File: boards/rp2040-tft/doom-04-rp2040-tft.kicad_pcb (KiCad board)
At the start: 4 copper layers, 132 x 58 mm, 79 parts, among them J2 S2B-PH-K-S(LF)(SN), J4 DM3AT-SF-PEJM5, J5 S2B-PH-K-S(LF)(SN), Q1 FS8205A, SW9 JS102011SAQN, U1 RP2040, U2 TP4056, U3 DW01A, U4 TLV75533PDBVR, U5 PAM8403DR, U6 W25Q128JVSIQ, U7 ESD 2-line, Y1 12MHz 10pF

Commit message: PCBKit's mark and pcbkit.io on every board; the RP2350 handheld ready to order
The handheld runs from two 18650 cells in parallel behind a DW01A protector and a reverse-cell
P-MOSFET, charged at up to 500 mA from the Pico's USB-C by a BQ24075 (power path into VSYS, timers
off for 6 Ah), with an on/off switch on 3V3_EN, M3 holes, ground pours and the console on pads.
Every assembled part has a JLCPCB code in stock (Basic where there is one); the module sockets are
in the BOM, the modules listed in the order's README. Check complete, the ready review clean.
Every board: routed and checked complete with the new mark.
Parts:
- added logo: , Logo_PCBKit_pcbkit.io, F.Cu at (127.8, 194.8)
- SW1, SW10, SW2, SW3, SW4, SW5, SW6, SW7, SW8: value (none) -> PTS645SM43SMTR92 LFS

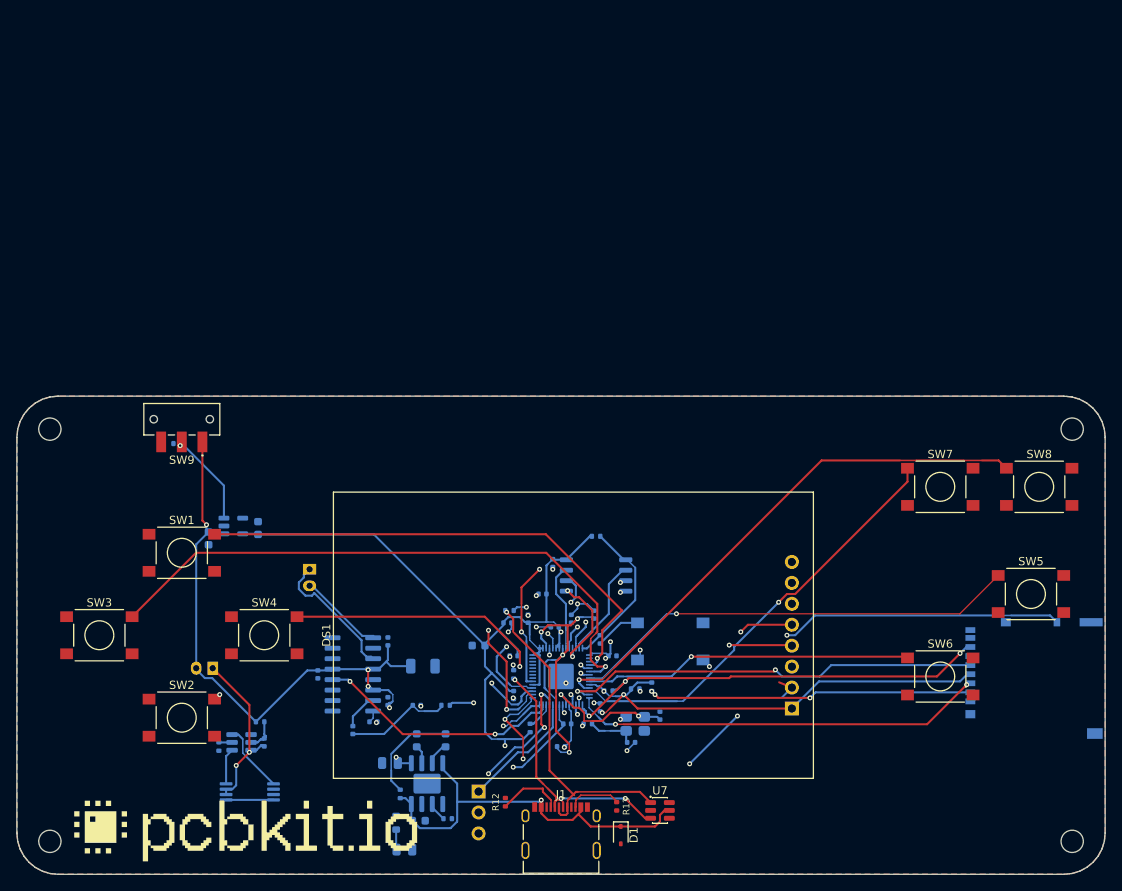
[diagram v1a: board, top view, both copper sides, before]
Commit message: rp2040-tft: two 18650 cells with protection and a USB-C charger; every part orderable
The LiPo and TP4056 become two 18650 in parallel (Keystone 1042 holders on the back) behind a
reverse-cell P-FET and DW01A + FS8205A, charged by a BQ24075 with power path from the board's
USB-C (1 A PTC and TVS on VBUS), SYS feeding the LDO and the amplifier (as rp2350-handheld).
BOOT and RESET buttons by the USB-C for the boot ROM's UF2 loader; the RP2040's decoupling within
3 mm of each supply pin; the speaker connector on the edge; board 132 x 104 mm, M3 holes, test
pads; every assembled part pinned to an LCSC code.
check: complete, 0 errors (4 USB-pair warnings, justified); ready lens: nothing to fix; fab
export without --force.

Claude-Session: https://claude.ai/code/session_01ATmMmxyrWxFwR3nTdXUrcx
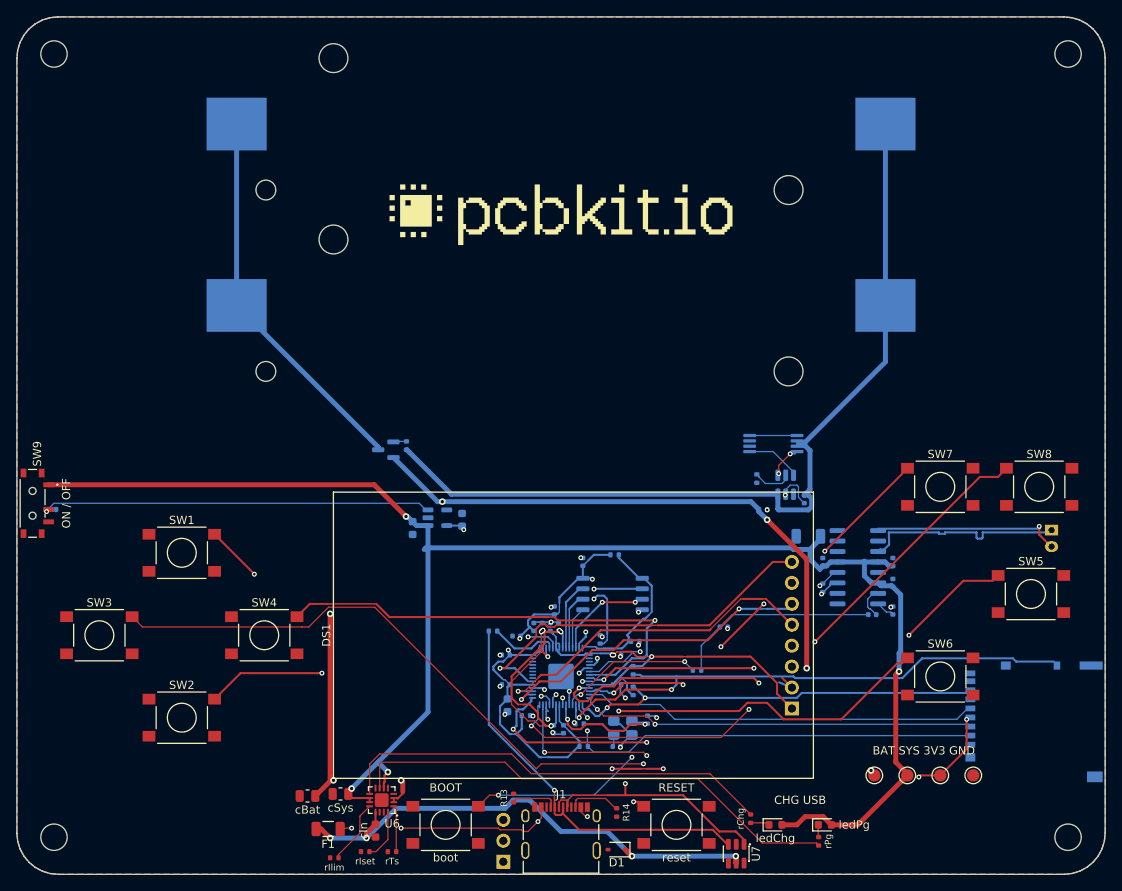
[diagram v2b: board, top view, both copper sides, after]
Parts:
- removed C20: 10uF, C_0805_2012Metric
- removed C21: 100nF, C_0402_1005Metric
- removed C8: 1uF, C_0603_1608Metric
- removed D2: red, LED_0603_1608Metric
- removed D3: green, LED_0603_1608Metric
- removed J2: S2B-PH-K-S(LF)(SN), JST_PH_S2B-PH-K_1x02_P2.00mm_Horizontal
- removed R18, R5: 1kohm, R_0402_1005Metric
- removed SW10: PTS645SM43SMTR92 LFS, SW_Tactile_SPST_6x6mm_SMD
- added BT1: 1042, BatteryHolder_Keystone_1042_1x18650, B.Cu at (166.0, 131.0)
- added BT2: 1042, BatteryHolder_Keystone_1042_1x18650, B.Cu at (166.0, 109.0)
- added F1: PTC 1000mA, Fuse_1206_3216Metric, F.Cu at (137.8, 194.5)
- added Q2: FS8205A, TSSOP-8_4.4x2.93mm_P0.65mm, B.Cu at (191.8, 147.8)
- added boot: PTS645SM43SMTR92 LFS, SW_Tactile_SPST_6x6mm_SMD, F.Cu at (152.0, 194.0)
- added cBat: 4.7uF, C_0805_2012Metric, F.Cu at (135.2, 190.5)
- added cIn: 1uF, C_0603_1608Metric, F.Cu at (143.5, 194.7)
- added cSys: 4.7uF, C_0805_2012Metric, F.Cu at (139.2, 190.2)
- added ledChg: red, LED_0603_1608Metric, F.Cu at (192.0, 194.0)
- added ledPg: green, LED_0603_1608Metric, F.Cu at (198.0, 194.0)
- added rBoot: 1kohm, R_0402_1005Metric, B.Cu at (175.0, 171.8)
- added rChg: 1.5kohm, R_0402_1005Metric, F.Cu at (189.0, 193.2)
- added rIlim: 1.18kohm, R_0402_1005Metric, F.Cu at (138.5, 198.0)
- added rIset: 1.13kohm, R_0402_1005Metric, F.Cu at (142.2, 197.2)
- added rPg: 1.5kohm, R_0402_1005Metric, F.Cu at (197.2, 196.0)
- added rTs: 10kohm, R_0402_1005Metric, F.Cu at (145.5, 197.2)
- added reset: PTS645SM43SMTR92 LFS, SW_Tactile_SPST_6x6mm_SMD, F.Cu at (180.0, 194.0)
- added tpBat: , TestPoint_Round_D1.5mm, F.Cu at (204.0, 188.0)
- added tpGnd: , TestPoint_Round_D1.5mm, F.Cu at (216.0, 188.0)
- added tpSys: , TestPoint_Round_D1.5mm, F.Cu at (208.0, 188.0)
- added tpV3: , TestPoint_Round_D1.5mm, F.Cu at (212.0, 188.0)
- C19: value 10uF -> 100nF; footprint C_0805_2012Metric -> C_0402_1005Metric
- H1, H2, H3, H4: footprint MountingHole_2.7mm_M2.5 -> MountingHole_3.2mm_M3
- Q1: value FS8205A -> AO3401A; footprint TSSOP-8_4.4x2.93mm_P0.65mm -> SOT-23
- R12: value 5.1kohm -> 100kohm; moved to B.Cu
- R14: value 1ohm -> 5.1kohm; footprint R_0603_1608Metric -> R_0402_1005Metric; moved to F.Cu
- R15: value 1.2kohm -> 100kohm
- R16: value 1kohm -> 100ohm
- R17: value 100ohm -> 1kohm
- SW9: value JS102011SAQN -> MSK12C02; footprint SW_Slide_SPDT_CK_JS102011SAQN_Horizontal -> SW_Slide_SPDT_Shouhan_MSK12C02
- U2: value TP4056 -> DW01A; footprint SOIC-8-1EP_3.9x4.9mm_P1.27mm_EP2.413x3.302mm -> SOT-6_1.6x2.9mm_P0.95mm
- U3: value DW01A -> W25Q128JVSIQ; footprint SOT-6_1.6x2.9mm_P0.95mm -> SOIC-8_5.23x5.28mm_P1.27mm
- U6: value W25Q128JVSIQ -> BQ24075RGTR; footprint SOIC-8_5.23x5.28mm_P1.27mm -> QFN-16-1EP_3x3mm_P0.5mm_EP1.68x1.68mm; moved to F.Cu
- moved J5 90.1 mm to (225.5, 159.2)
- moved logo 84.0 mm to (166.0, 120.0)
- moved R17 67.1 mm to (189.8, 152.0), turned to 90 degrees
- moved C29 64.5 mm to (203.8, 168.5), turned to 180 degrees
- moved C19 64.5 mm to (195.5, 154.5), turned to 270 degrees
- moved C28 64.4 mm to (206.2, 168.0), turned to 270 degrees
- moved C24 62.9 mm to (206.2, 164.7)
- moved C26 62.7 mm to (197.8, 162.1), turned to 270 degrees
- moved U5 62.6 mm to (202.0, 162.8)
- moved C25 62.0 mm to (206.2, 162.1)
- moved U2 56.6 mm to (193.2, 152.8), turned to 90 degrees
- moved R16 55.9 mm to (190.5, 155.8), turned to 180 degrees
- moved C27 49.3 mm to (196.0, 159.0), turned to 0 degrees
- moved U3 48.5 mm to (172.2, 166.0), turned to 0 degrees
- moved R12 46.5 mm to (197.8, 165.2)
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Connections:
- net Net-(C11-1) renamed DVDD
- C19 pad 1: U2Support/C1_P -> Net-(C19-1)
- C19 pad 2: GND -> CELL_N
- C22 pad 1: VBAT -> SYS
- C24 pad 1: VBAT -> SYS
- C25 pad 1: VBAT -> SYS
- C26 pad 1: VBAT -> SYS
- C27 pad 1: VBAT -> SYS
- C29 pad 1: Net-(C29-1) -> AUDIO
- C29 pad 2: AUDIO -> Net-(C29-1)
- J1 pad A4: VBUS -> usb/power/raw
- J1 pad B4: VBUS -> usb/power/raw
- Q1 pad 1: U3Support/DRAIN -> reversed/gate
- Q1 pad 2: BAT_N -> BAT
- Q1 pad 3: BAT_N -> BAT_IN
- R12 pad 1: usb/power/cc1 -> AMP_SD
- R13 pad 1: usb/power/cc2 -> usb/power/cc1
- R14 pad 1: VBUS -> usb/power/cc2
- R14 pad 2: U2Support/C1_P -> GND
- R15 pad 1: Net-(R15-1) -> CELL_N
- R15 pad 2: GND -> reversed/gate
- R16 pad 1: U2Support/LED_A -> BAT
- R16 pad 2: VBUS -> Net-(C19-1)
- R17 pad 1: Net-(C21-1) -> Net-(R17-1)
- R17 pad 2: VBAT -> GND
- R6 pad 1: Net-(R6-1) -> V3
- R6 pad 2: V3 -> RUN
- R8 pad 1: SD_CS -> V3
- R8 pad 2: V3 -> SD_CS
- R9 pad 1: SD_MISO -> V3
- R9 pad 2: V3 -> SD_MISO
- SW9 pad 1: VBAT -> SYS
- SW9 pad 3: GND -> (no net)
- U1 pad 26: Net-(R6-1) -> RUN
- U2 pad 1: GND -> Net-(Q2-4)
- U2 pad 2: Net-(R15-1) -> Net-(R17-1)
- U2 pad 3: GND -> Net-(Q2-5)
- U2 pad 4: VBUS -> (no net)
- U2 pad 5: VBAT -> Net-(C19-1)
- U2 pad 6: Net-(D3-1) -> CELL_N
- U3 pad 1: Net-(Q1-4) -> Net-(R4-1)
- U3 pad 2: Net-(R18-1) -> Net-(U1-55)
- U3 pad 3: Net-(Q1-5) -> Net-(U1-54)
- U3 pad 4: (no net) -> GND
- U3 pad 5: Net-(C21-1) -> Net-(U1-53)
- U3 pad 6: BAT_N -> Net-(U1-52)
- U4 pad 1: VBAT -> SYS
- U5 pad 13: VBAT -> SYS
- U5 pad 4: VBAT -> SYS
- U5 pad 6: VBAT -> SYS
- U6 pad 1: Net-(R4-1) -> TS
- U6 pad 2: Net-(U1-55) -> BAT
- U6 pad 3: Net-(U1-54) -> BAT
- U6 pad 5: Net-(U1-53) -> GND
- U6 pad 6: Net-(U1-52) -> SYS
- U6 pad 7: Net-(U1-51) -> PG_N
- U6 pad 8: V3 -> GND
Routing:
- net SYS: track 0.00 -> 200.8 mm, vias 0 -> 4
- net BAT: track 0.00 -> 138.6 mm, vias 0 -> 7
- net CELL_N: track 0.00 -> 105.7 mm
- net VBAT: track 86.1 -> 0.00 mm, vias 5 -> 0
- net PG_N: track 0.00 -> 60.5 mm
- net CHG_N: track 0.00 -> 53.4 mm
- net BAT_IN: track 0.00 -> 46.6 mm
- net BOOTSEL: track 0.00 -> 35.7 mm, vias 0 -> 3
- net LDO_EN: track 11.2 -> 46.8 mm
- net usb/power/raw: track 0.00 -> 34.5 mm, vias 0 -> 4
- net BAT_N: track 23.1 -> 0.00 mm, vias 2 -> 0
- net AMP_SD: track 30.1 -> 51.8 mm, vias 2 -> 3
- net RUN: track 0.00 -> 19.5 mm, vias 0 -> 3
- net LEFT: track 73.7 -> 92.8 mm, vias 1 -> 2
- net V3: track 186.5 -> 169.5 mm, vias 8 -> 9
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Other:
- board size 132 x 58 mm -> 132 x 104 mm
- board text added: "+"
- board text added: "-"
- board text added: "2 x 18650 Li-ion 3.7 V"
- board text added: "BAT SYS 3V3 GND"
- board text added: "BOOT"
- board text added: "CHG USB"
- board text added: "ON / OFF"
- board text added: "RESET"
